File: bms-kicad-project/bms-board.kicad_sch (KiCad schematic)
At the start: 0 parts

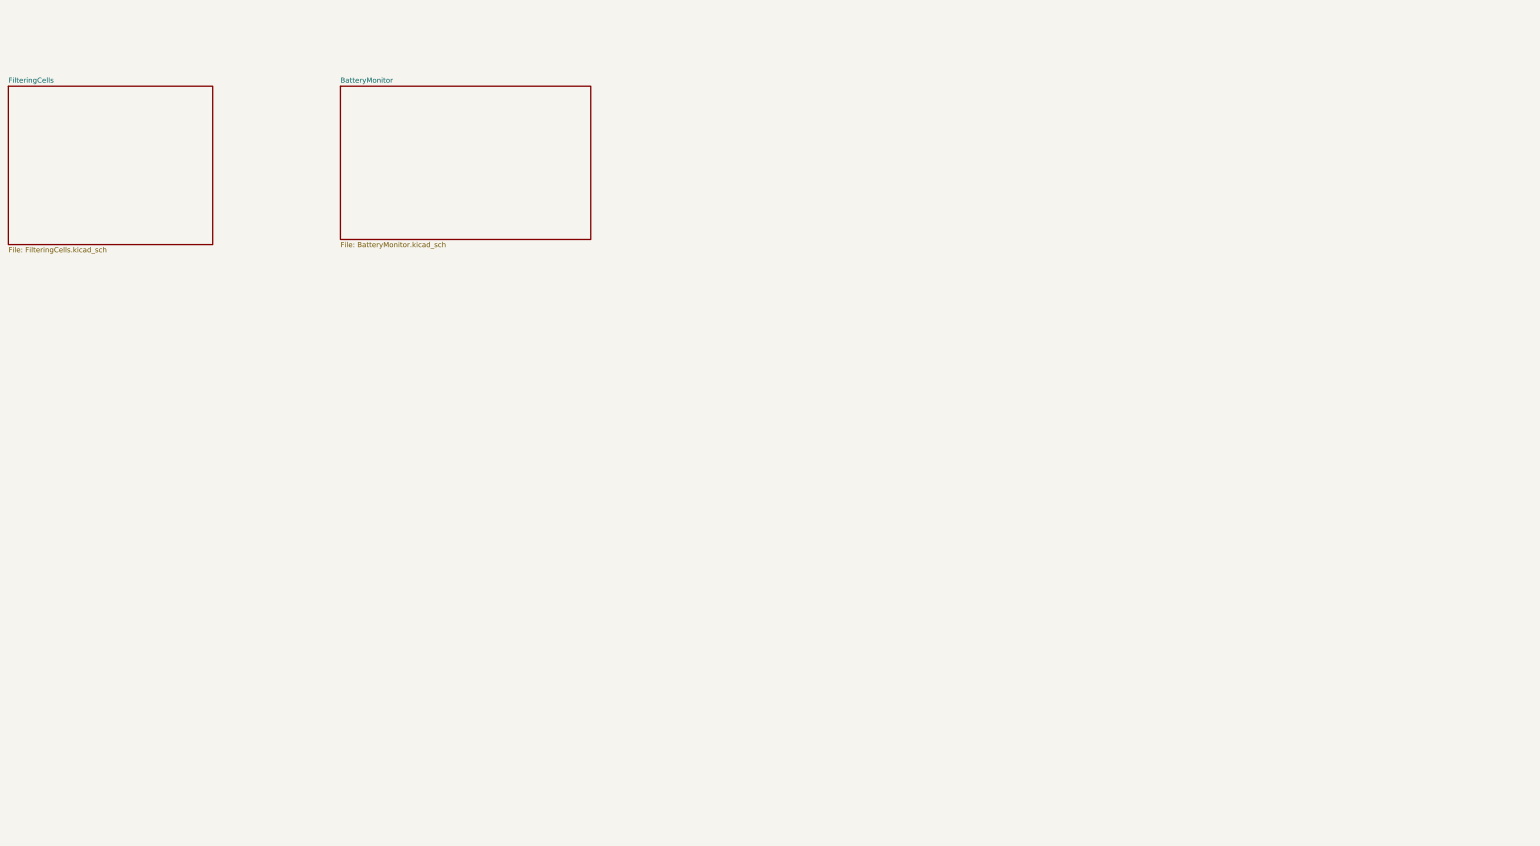
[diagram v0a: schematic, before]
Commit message: Feature: Add RP2040 MCU, folder for 3D models of components, continuing edits on other schematics (#15)
* hierarchical label conversion and readability changes

* feat: added minimal MCU schematic, 3D component model folder

* feat:continuing work on integrating RP2040 MCU

* feat: Added 3D models for connector and Flash ROM

* Added 3D Models in Cell Filtering and Balancing Sch.

* feat. Added most 3D models for footprints

* feat: continuing work on MCU circuit

* feat: finished preliminary RP2040 schematic design

---------

Co-authored-by: Dhruv Dingari <dingari.d@northeastern.edu>
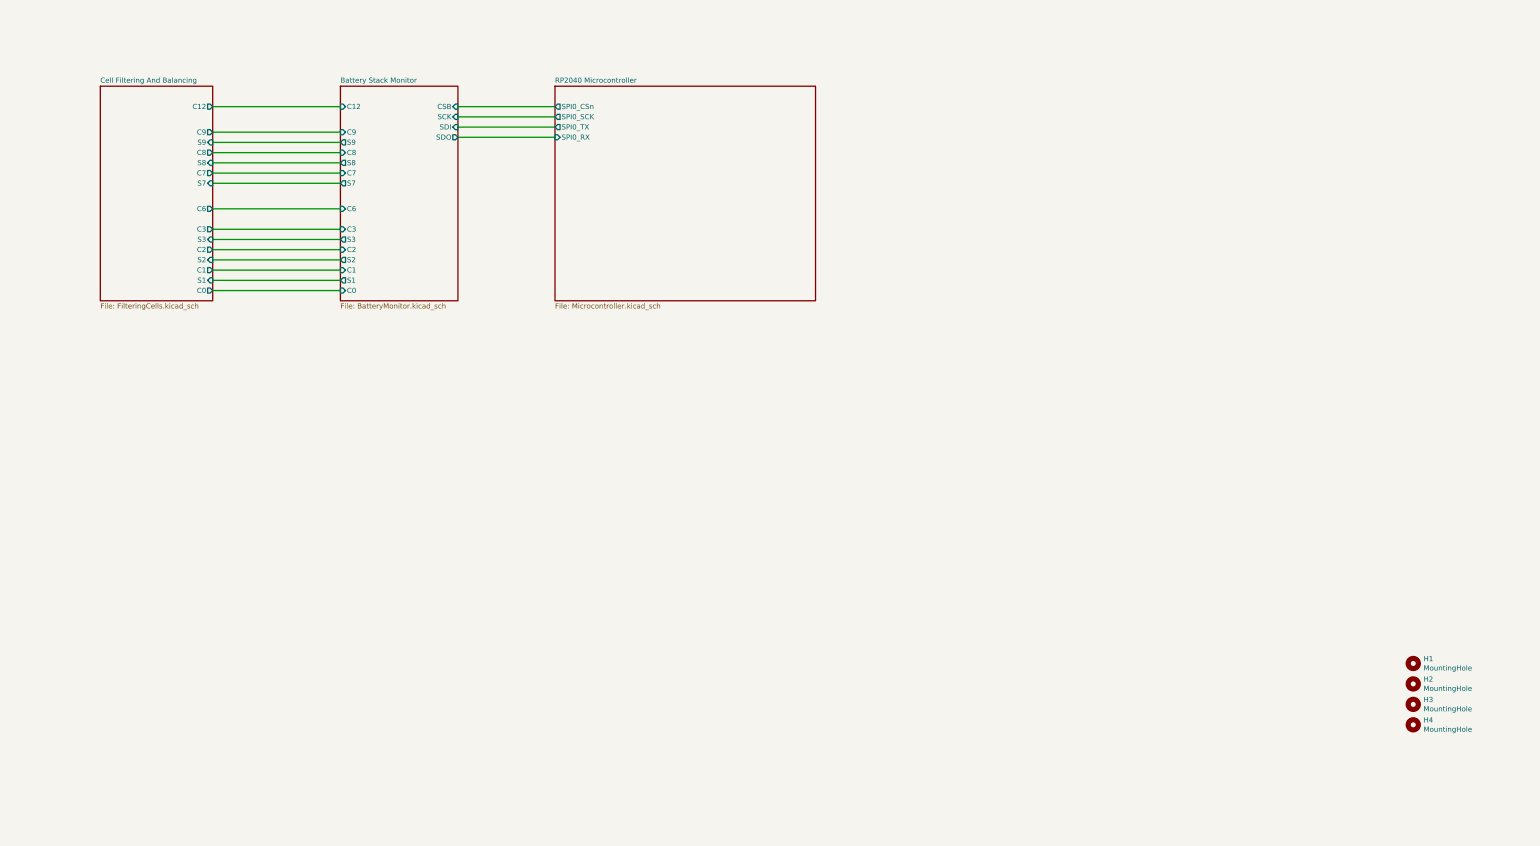
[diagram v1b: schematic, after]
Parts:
- added H1, H2, H3, H4: MountingHole, MountingHole:MountingHole_2.7mm_M2.5, symbol Mechanical:MountingHole
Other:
- sheet BatteryMonitor renamed Battery Stack Monitor
- sheet FilteringCells renamed Cell Filtering And Balancing
- added sheet RP2040 Microcontroller (Microcontroller.kicad_sch)
- sheet Battery Stack Monitor ports: added C0, C1, C12, C2, C3, C6, C7, C8, C9, CSB, S1, S2, S3, S7, S8, S9, SCK, SDI, SDO; removed none
- sheet Cell Filtering And Balancing ports: added C0, C1, C12, C2, C3, C6, C7, C8, C9, S1, S2, S3, S7, S8, S9; removed none
- company: (none) -> AeroNU - FixedWing
- title: (none) -> Top-Level Interconnect

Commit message: Feature: Added schematic and symbols for 5V switching regulator (#16)
* feat: initial 5V-reg-and-edits branch commit

* feat: small to-do list edits

* feat: put filtering and balancing circuits into hierarchical format

* feat: forgot to commit smol change

* feat: Added SiC461 Schematic, Footprint, and 3D Model

* feat: Added all components listed in the spreadsheet, until Inductor L1

* feat: forgor the description

* feat: Added all symbols and 3D models. Also began working on Regulator Schematic.

* feat: Added more connections to the 5V Regulator schematic.

* feat: Added VFB connection in 5V Regulator Schematic

* feat: Added 220uf cap & modified 5V Reg Circuit

* feat: Added more to 5V Regulator Schematic

* feat: Changed all resistor symbols to be the standard KiCAD symbol, started improving schematic.

* feat: Forgot to save changes to schematic.

* feat: Just about completed 5V Regulator Schematic.

* feat: cosmetic changes to 5V reg schematic

* feat: Added comment boxes and fixed 5V Regulator Schematic.

* feat: just moved around and edited notes on the 5V reg schematic

* feat: re-ordered page numbers

* feat: Added snubber circuit to 5V Regulator schematic

* feat: Added 0OHM jumper between ULTRASONIC and VDD, added LED indicator for PGOOD

* feat: added buncha shit, refer to tasks 4 and 8

* feat: finished 5V reg circuit lgtm!

---------

Co-authored-by: cowman19 <matthewf9001@gmail.com>
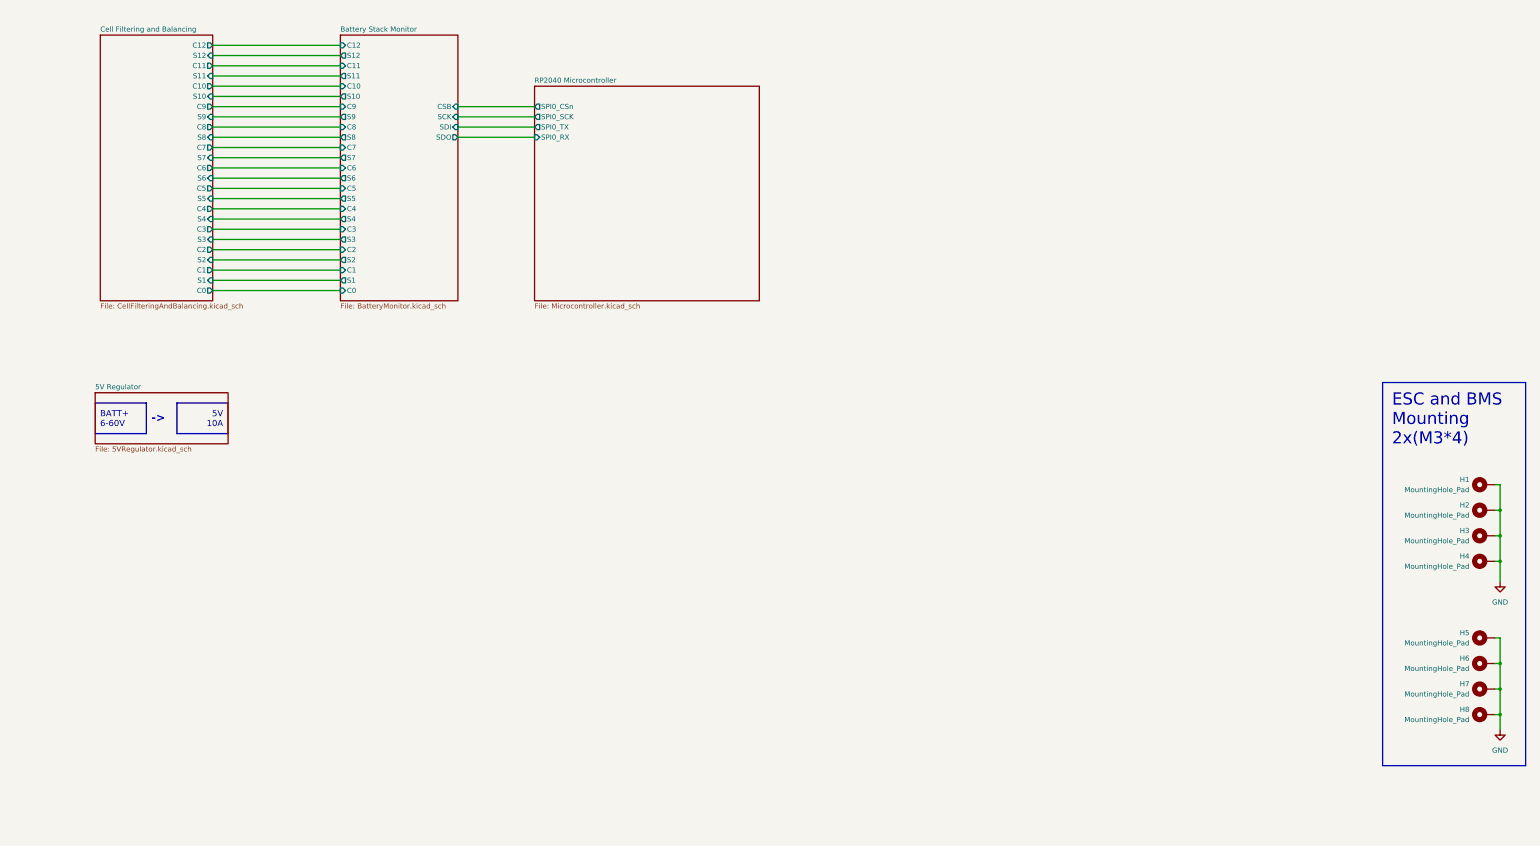
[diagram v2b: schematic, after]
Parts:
- removed H1, H2, H3, H4: MountingHole, MountingHole:MountingHole_2.7mm_M2.5, symbol Mechanical:MountingHole
- added H1, H2, H3, H4, H5, H6, H7, H8: MountingHole_Pad, MountingHole:MountingHole_3.2mm_M3_Pad_Via, symbol Mechanical:MountingHole_Pad
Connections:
- new net GND: H1.1, H2.1, H3.1, H4.1, H5.1, H6.1, H7.1, H8.1
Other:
- sheet Cell Filtering And Balancing renamed Cell Filtering and Balancing
- added sheet 5V Regulator (5VRegulator.kicad_sch)
- sheet Battery Stack Monitor ports: added C10, C11, C4, C5, S10, S11, S12, S4, S5, S6; removed none
- sheet Cell Filtering and Balancing: file FilteringCells.kicad_sch -> CellFilteringAndBalancing.kicad_sch
- sheet Cell Filtering and Balancing ports: added C10, C11, C4, C5, S10, S11, S12, S4, S5, S6; removed none
- note added: "->"

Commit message: Feature/current sensor (#17)
* feat: making sure my git still works

* feat: figured out battery stack monitor V+ biasing. Refer to task 5 on the punchlist for more details.

* feat: swapped out battery<->18V diode for cheaper alternative

* feat: started a new sheet for external connections and added current sensor

* feat: made a placeholder label to connect current sensor to LTC6811 GPIO

* feat: added remaining connectors to component library

* Wired up most external connections

* feat: Just shifting a few things around
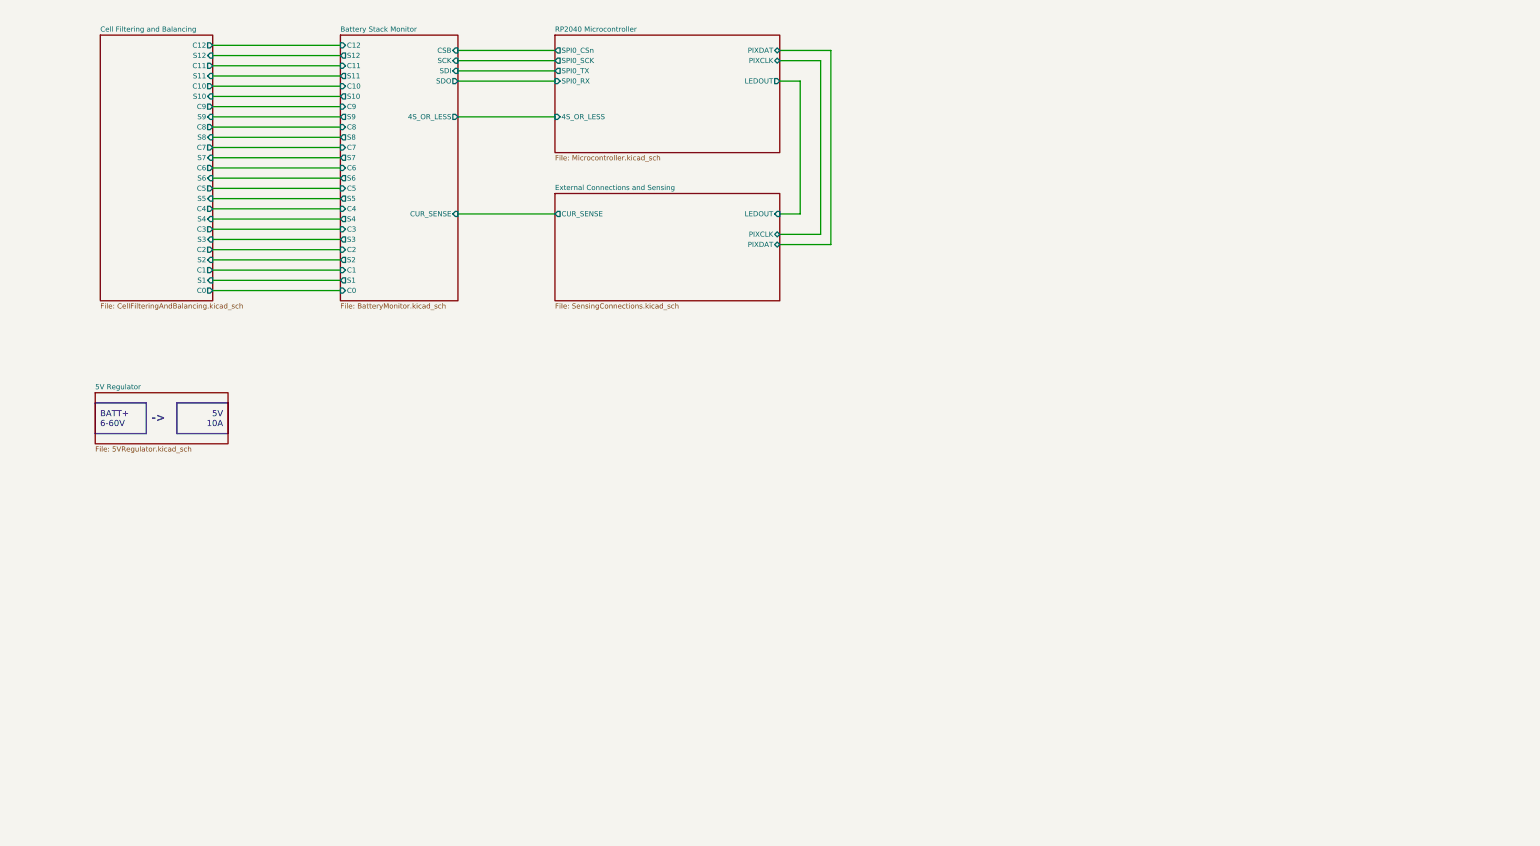
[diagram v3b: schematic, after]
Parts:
- removed H1, H2, H3, H4, H5, H6, H7, H8: MountingHole_Pad, MountingHole:MountingHole_3.2mm_M3_Pad_Via, symbol Mechanical:MountingHole_Pad
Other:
- added sheet External Connections and Sensing (SensingConnections.kicad_sch)
- sheet Battery Stack Monitor ports: added 4S_OR_LESS, CUR_SENSE; removed none
- sheet RP2040 Microcontroller ports: added 4S_OR_LESS, LEDOUT, PIXCLK, PIXDAT; removed none

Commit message: Feature/library migration (#19)
* feat: first library migration commit

* feat: added sims directory, new cell balancing components

* feat: cell filtering/balancing switchover done

* feat: don't even know what I changed, just zoned out for several hours. Made PCB r/a mount XT-60s and solder pads into a 2-for-1 deal

* feat: schematic pretty much done

* feat: started layout

* feat: added current sense DAC

* feat: added capacitors to DAC

* feat:added more capacitors to DAC

* feat: more DAC capacitors

* feat: added temp sensor symbol/footprint

* added temp sense cad models

* feat: Added temp sensors

* feat: schematic cleanup, continued layout

* feat: added tvs protection ic to usb

* feat: placing cell filtering/balancing components

* feat: lotta layout

* feat: cell balancing board

* feat: changed cell balancing schem

* feat: slightly edited cell balance schem

* feat: big pre-design review schematic commit

* feat: post-design review clarity

* feat: I am so tired. 4-layer layout almost done

* feat: biiig layout and slight design change commit

* feat:bos->lax layout sesh

* feat: lax -> syd layout sesh

* feat: DRC run

* feat: deleted manufacturing files

* feat: silkscreen done

* feat: REV A COMMIT FOR FAB

* doc: updated schematic docs

---------

Co-authored-by: Ronan Gleason <gleason.r@northeastern.edu>
Co-authored-by: cassidysakamoto <sakamoto.ca@northeastern.edu>
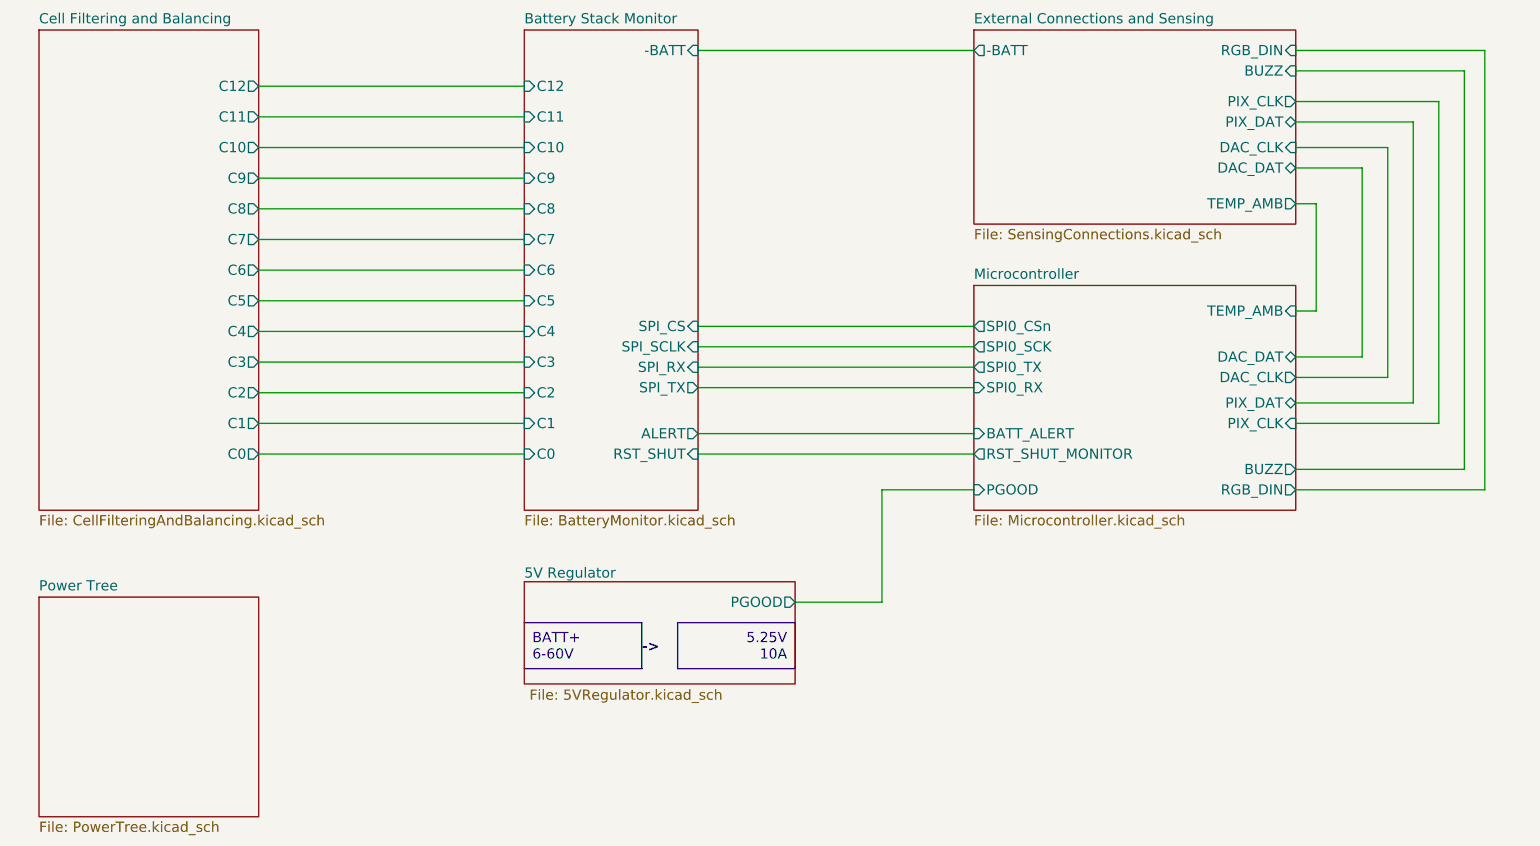
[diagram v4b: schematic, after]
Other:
- sheet RP2040 Microcontroller renamed Microcontroller
- added sheet Power Tree (PowerTree.kicad_sch)
- sheet 5V Regulator ports: added PGOOD; removed none
- sheet Battery Stack Monitor ports: added -BATT, ALERT, RST_SHUT, SPI_CS, SPI_RX, SPI_SCLK, SPI_TX; removed 4S_OR_LESS, CSB, CUR_SENSE, S1, S10, S11, S12, S2, S3, S4, S5, S6, S7, S8, S9, SCK, SDI, SDO
- sheet Cell Filtering and Balancing ports: added none; removed S1, S10, S11, S12, S2, S3, S4, S5, S6, S7, S8, S9
- sheet External Connections and Sensing ports: added -BATT, BUZZ, DAC_CLK, DAC_DAT, PIX_CLK, PIX_DAT, RGB_DIN, TEMP_AMB; removed CUR_SENSE, LEDOUT, PIXCLK, PIXDAT
- sheet Microcontroller ports: added BATT_ALERT, BUZZ, DAC_CLK, DAC_DAT, PGOOD, PIX_CLK, PIX_DAT, RGB_DIN, RST_SHUT_MONITOR, TEMP_AMB; removed 4S_OR_LESS, LEDOUT, PIXCLK, PIXDAT
